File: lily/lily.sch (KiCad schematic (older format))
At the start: 23 parts, among them J1 NEIGHBOR1, J10 TEST_2P, J2 NEIGHBOR2, J3 ANT_IN, J4 TEST_2P, J5 TEST_2P, J6 TEST_2P, J7 BONUS_ROW, J8 TEST_2P, J9 TEST_2P, U1 ADL5904

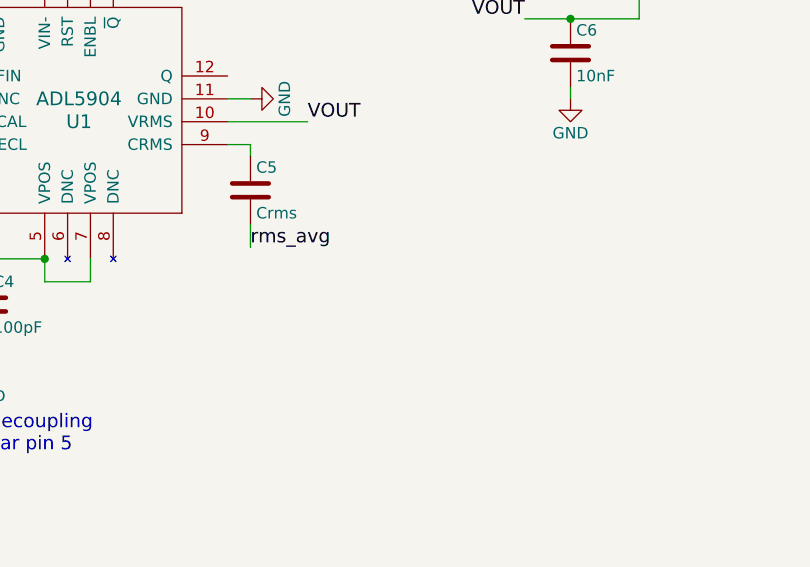
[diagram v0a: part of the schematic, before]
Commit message: Updated copper pours on Lily PCB layout, added comments on schematic.
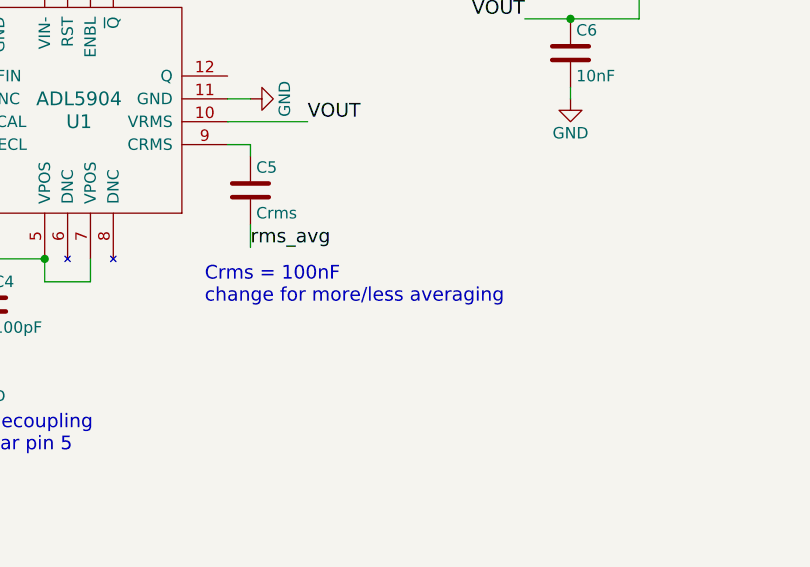
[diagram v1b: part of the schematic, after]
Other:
- note added: "Crms = 100nF\nchange for more/less averaging"
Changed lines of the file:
@@
 Text Label 8450 2250 2    60   ~ 0
 ENBL
+Text Notes 9750 5250 0    60   ~ 0
+Crms = 100nF\nchange for more/less averaging
 $EndSCHEMATC

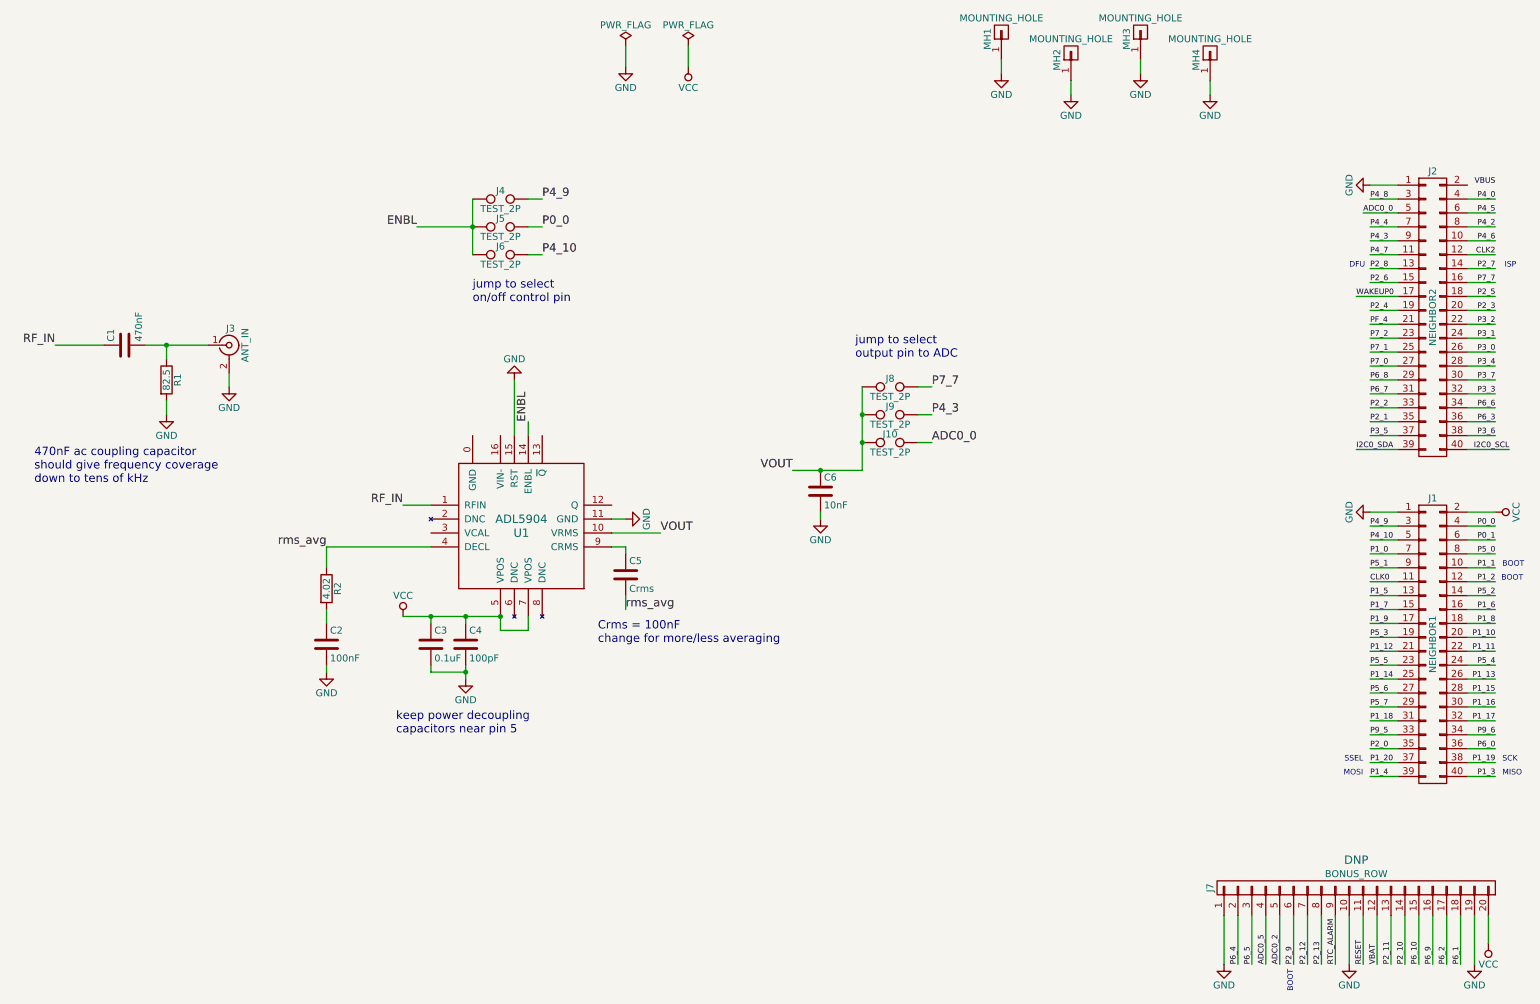
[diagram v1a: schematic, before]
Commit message: Revised Lily schematic and PCB: Added connections for threshold detection mode and improved RF impedance matching.
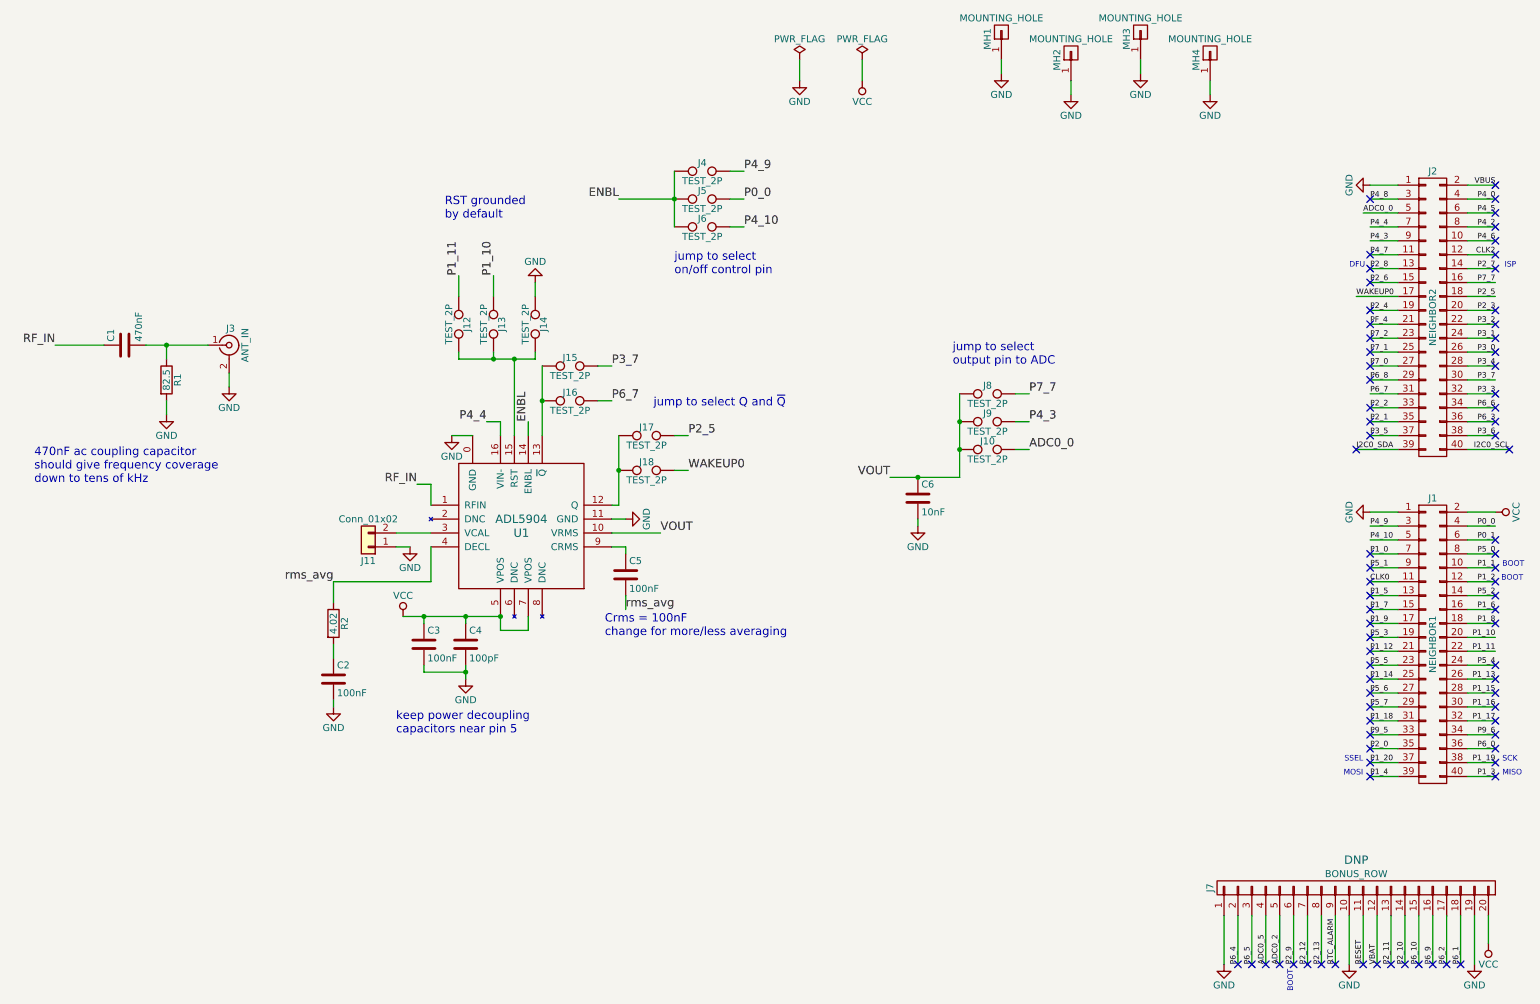
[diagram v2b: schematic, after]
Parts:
- added J11: Conn_01x02, Pin_Headers:Pin_Header_Straight_1x02_Pitch2.54mm, symbol Conn_01x02
- added J12, J13, J14, J15, J16, J17, J18: TEST_2P, gsg-modules:0603-JUMPER, symbol TEST_2P
- C1: Description (none) -> CAP CER 0.47UF 50V X5R 0603; Manufacturer (none) -> Murata Electronics North America; Part Number (none) -> GRM188R61H474KA12D
- C2: Description (none) -> CAP CER 0.1UF 50V X8L 0603; Manufacturer (none) -> Murata Electronics North America; Part Number (none) -> GCM188L81H104KA57D
- C3: value 0.1uF -> 100nF; Description (none) -> CAP CER 0.1UF 50V X8L 0603; Manufacturer (none) -> Murata Electronics North America; Part Number (none) -> GCM188L81H104KA57D
- C4: Description (none) -> CAP CER 100PF 50V C0G/NP0 0603; Manufacturer (none) -> Murata Electronics North America; Part Number (none) -> GQM1885C1H101JB01D
- C5: value Crms -> 100nF; Description (none) -> CAP CER 0.1UF 50V X8L 0603; Manufacturer (none) -> Murata Electronics North America; Part Number (none) -> GCM188L81H104KA57D
- C6: Description (none) -> CAP CER 10PF 50V C0G/NP0 0603; Manufacturer (none) -> Murata Electronics North America; Part Number (none) -> GQM1885C1H100JB01D
- J3: Description (none) -> CONN RPSMA RCPT STR 50OHM EDGEMT; Manufacturer (none) -> Linx Technologies Inc.; Part Number (none) -> CONREVSMA003.031
- R1: Description (none) -> RES 82.5 OHM 1% 1/10W 0603; Manufacturer (none) -> Stackpole Electronics Inc.; Part Number (none) -> RMCF0603FT82R5
- R2: Description (none) -> RES 4.02 OHM 1% 1/10W 0603; Manufacturer (none) -> Stackpole Electronics Inc.; Part Number (none) -> RMCF0603FT4R02
- U1: footprint gsg-modules:ADL5904 -> gsg-modules:QFN16-3; Description (none) -> RMS TRUPWR DETECTORS; Manufacturer (none) -> Analog Devices; Part Number (none) -> ADL5904ACPZN-R7
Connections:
- net GND: now also U1.0 (GND), J11.1 (Pin_1), J14.1; no longer U1.15 (RST)
- net P1_10: now also J13.1
- net P1_11: now also J12.1
- net P2_5: now also J17.2
- net P3_7: now also J15.2
- net P4_4: now also U1.16 (VIN-)
- net P6_7: now also J16.2
- net VBUS: now also J2.2 (P2)
- net WAKEUP0: now also J18.2
- net at U1.12 (Q): now also J17.1, J18.1
- net at U1.13 (~Q~): now also J15.1, J16.1
- net at U1.3 (VCAL): now also J11.2 (Pin_2)
- new net: J12.2, J13.2, J14.2, U1.15 (RST)
- no-connect marks 0 -> 80
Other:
- note added: "RST grounded\nby default"
- note added: "jump to select Q and ~Q~"
- moved on the sheet: C2, C3, C6, J10, J4, J5, J6, J8, J9, R2

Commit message: Revised Lily PCB: added silkscreen labels, rerouted tracks, etc.
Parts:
- C1: Description CAP CER 0.47UF 50V X5R 0603 -> CAP CER 0.47UF 50V X5R 0603
- C2, C3, C5: Description CAP CER 0.1UF 50V X8L 0603 -> CAP CER 0.1UF 50V X8L 0603
- C4: Description CAP CER 100PF 50V C0G/NP0 0603 -> CAP CER 100PF 50V C0G/NP0 0603
- C6: Description CAP CER 10PF 50V C0G/NP0 0603 -> CAP CER 10PF 50V C0G/NP0 0603
- R1: Description RES 82.5 OHM 1% 1/10W 0603 -> RES 82.5 OHM 1% 1/10W 0603
- R2: Description RES 4.02 OHM 1% 1/10W 0603 -> RES 4.02 OHM 1% 1/10W 0603
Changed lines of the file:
@@
 F 4 "Murata Electronics North America" H 8500 5250 60  0001 C CNN "Manufacturer"
 F 5 "GCM188L81H104KA57D" H 8500 5250 60  0001 C CNN "Part Number"
-F 6 "CAP CER 0.1UF 50V X8L 0603 " H 8500 5250 60  0001 C CNN "Description"
+F 6 "CAP CER 0.1UF 50V X8L 0603" H 8500 5250 60  0001 C CNN "Description"
 	1    8500 5250
 	1    0    0    -1
@@
 F 4 "Murata Electronics North America" H 8800 5250 60  0001 C CNN "Manufacturer"
 F 5 "GQM1885C1H101JB01D" H 8800 5250 60  0001 C CNN "Part Number"
-F 6 " CAP CER 100PF 50V C0G/NP0 0603 " H 8800 5250 60  0001 C CNN "Description"
+F 6 "CAP CER 100PF 50V C0G/NP0 0603" H 8800 5250 60  0001 C CNN "Description"
 	1    8800 5250
 	1    0    0    -1
@@
 F 4 "Stackpole Electronics Inc." V 6650 3350 60  0001 C CNN "Manufacturer"
 F 5 "RMCF0603FT82R5" V 6650 3350 60  0001 C CNN "Part Number"
-F 6 " RES 82.5 OHM 1% 1/10W 0603 " V 6650 3350 60  0001 C CNN "Description"
+F 6 "RES 82.5 OHM 1% 1/10W 0603" V 6650 3350 60  0001 C CNN "Description"
 	1    6650 3350
 	1    0    0    -1
@@
 F 4 "Murata Electronics North America" H 6350 3100 60  0001 C CNN "Manufacturer"
 F 5 "GRM188R61H474KA12D" H 6350 3100 60  0001 C CNN "Part Number"
-F 6 " CAP CER 0.47UF 50V X5R 0603 " H 6350 3100 60  0001 C CNN "Description"
+F 6 "CAP CER 0.47UF 50V X5R 0603" H 6350 3100 60  0001 C CNN "Description"
 	1    6350 3100
 	0    -1   -1   0
@@
 F 4 "Murata Electronics North America" H 12050 4200 60  0001 C CNN "Manufacturer"
 F 5 "GQM1885C1H100JB01D" H 12050 4200 60  0001 C CNN "Part Number"
-F 6 " CAP CER 10PF 50V C0G/NP0 0603 " H 12050 4200 60  0001 C CNN "Description"
+F 6 "CAP CER 10PF 50V C0G/NP0 0603" H 12050 4200 60  0001 C CNN "Description"
 	1    12050 4200
 	1    0    0    -1
@@
 F 4 "Stackpole Electronics Inc." V 7850 5100 60  0001 C CNN "Manufacturer"
 F 5 "RMCF0603FT4R02" V 7850 5100 60  0001 C CNN "Part Number"
-F 6 " RES 4.02 OHM 1% 1/10W 0603 " V 7850 5100 60  0001 C CNN "Description"
+F 6 "RES 4.02 OHM 1% 1/10W 0603" V 7850 5100 60  0001 C CNN "Description"
 	1    7850 5100
 	1    0    0    -1
@@
 F 4 "Murata Electronics North America" H 7850 5500 60  0001 C CNN "Manufacturer"
 F 5 "GCM188L81H104KA57D" H 7850 5500 60  0001 C CNN "Part Number"
-F 6 "CAP CER 0.1UF 50V X8L 0603 " H 7850 5500 60  0001 C CNN "Description"
+F 6 "CAP CER 0.1UF 50V X8L 0603" H 7850 5500 60  0001 C CNN "Description"
 	1    7850 5500
 	1    0    0    -1
@@
 F 4 "Murata Electronics North America" H 9950 4750 60  0001 C CNN "Manufacturer"
 F 5 "GCM188L81H104KA57D" H 9950 4750 60  0001 C CNN "Part Number"
-F 6 " CAP CER 0.1UF 50V X8L 0603 " H 9950 4750 60  0001 C CNN "Description"
+F 6 "CAP CER 0.1UF 50V X8L 0603" H 9950 4750 60  0001 C CNN "Description"
 	1    9950 4750
 	1    0    0    -1

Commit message: Corrected Lily BOM
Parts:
- C6: Description CAP CER 10PF 50V C0G/NP0 0603 -> CAP CER 10000PF 25V X7R 0603; Manufacturer Murata Electronics North America -> Wurth Electronics Inc.; Part Number GQM1885C1H100JB01D -> 885012206065
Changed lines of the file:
@@
 F 2 "gsg-modules:0603" H 12088 4050 50  0001 C CNN
 F 3 "" H 12050 4200 50  0001 C CNN
-F 4 "Murata Electronics North America" H 12050 4200 60  0001 C CNN "Manufacturer"
-F 5 "GQM1885C1H100JB01D" H 12050 4200 60  0001 C CNN "Part Number"
-F 6 "CAP CER 10PF 50V C0G/NP0 0603" H 12050 4200 60  0001 C CNN "Description"
+F 4 "Wurth Electronics Inc." H 12050 4200 60  0001 C CNN "Manufacturer"
+F 5 "885012206065" H 12050 4200 60  0001 C CNN "Part Number"
+F 6 "CAP CER 10000PF 25V X7R 0603" H 12050 4200 60  0001 C CNN "Description"
 	1    12050 4200
 	1    0    0    -1
